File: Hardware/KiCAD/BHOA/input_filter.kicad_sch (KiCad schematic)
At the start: 5 parts

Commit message: added outpout relays
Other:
- company: (none) -> C Audio
- title: (none) -> BHOA
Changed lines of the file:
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@@
 (kicad_sch (version 20230121) (generator eeschema)
-  (paper "A5")
+  (paper "A4")
+  (title_block
+    (title "BHOA")
+    (rev "0.1")
+    (company "C Audio")
+    (comment 3 "Balanced Headphone Operationsal Amplifier")
+  )
   (junction (at 118.11 43.815) (diameter 0) (color 0 0 0 0)
   )

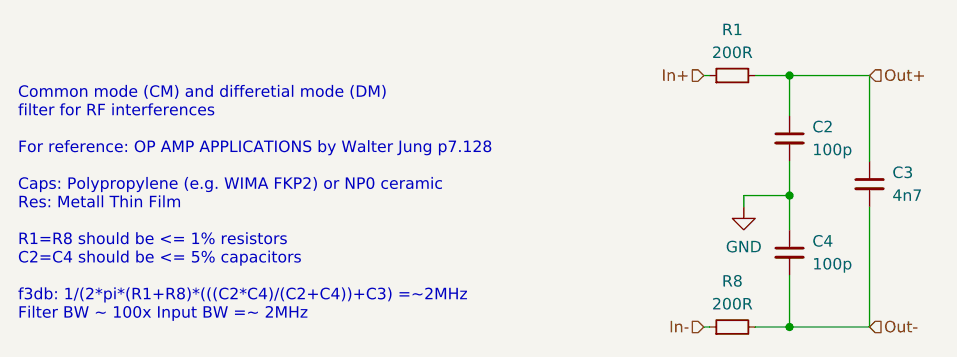
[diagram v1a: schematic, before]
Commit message: Updated PCB with output protection
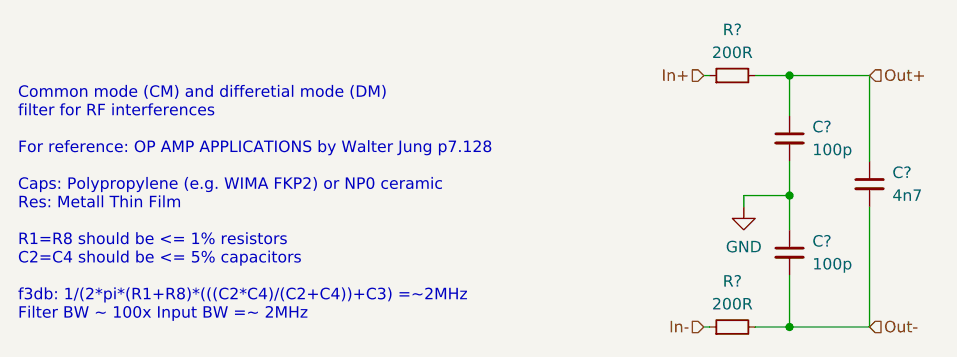
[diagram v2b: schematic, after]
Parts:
- renumbered C2 to C?, C4 to C?, C3 to C?, R8 to R?, R1 to R?
